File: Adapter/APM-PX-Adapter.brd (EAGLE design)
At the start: 22.9 x 20.3 mm, 13 parts, among them Q1 BSS138, Q2 BSS138

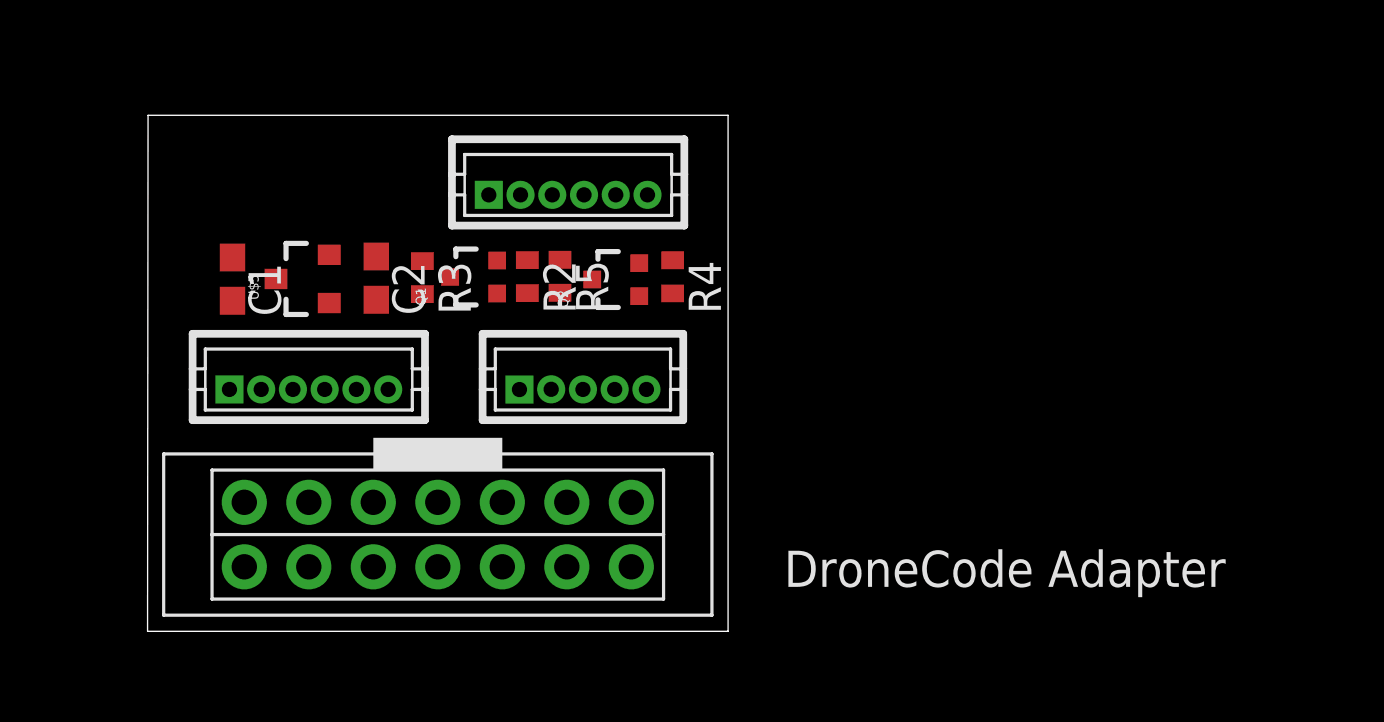
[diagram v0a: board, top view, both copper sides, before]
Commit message: Removed level shifting and switch to all through hole components. Ordering a prototype.
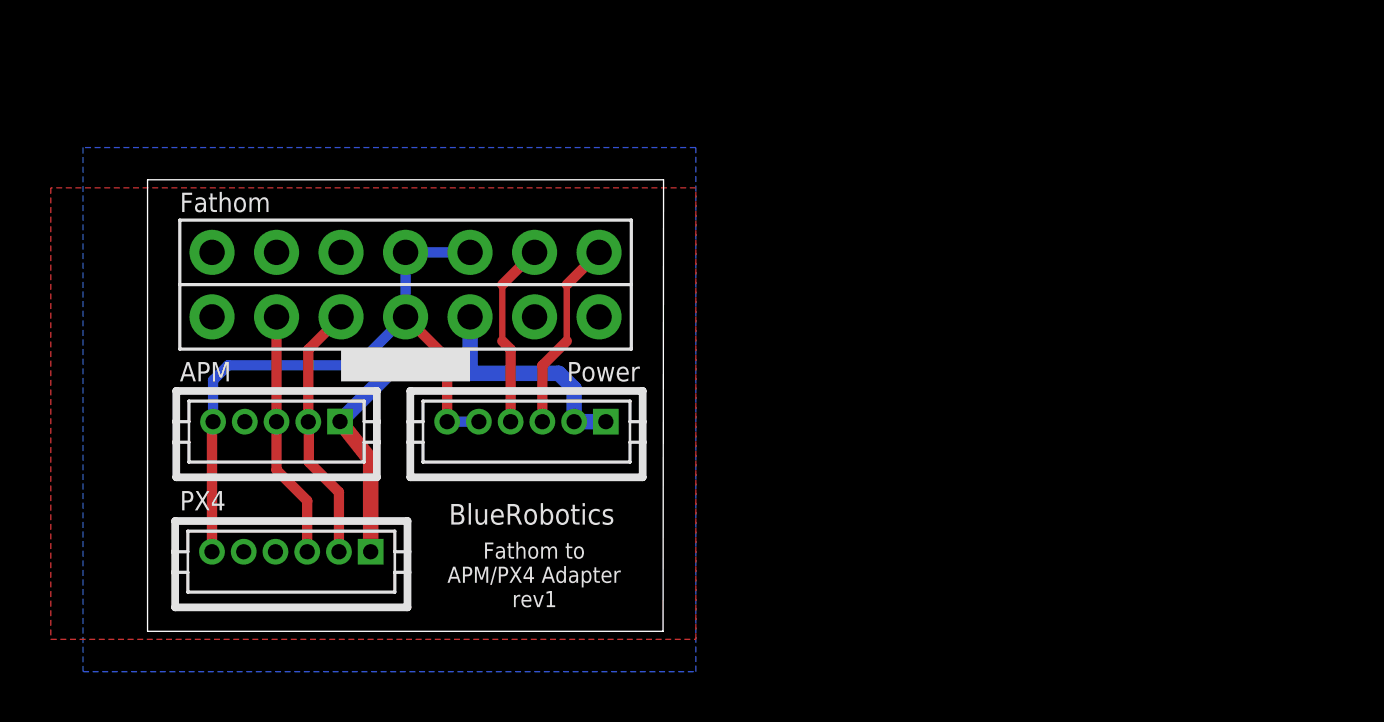
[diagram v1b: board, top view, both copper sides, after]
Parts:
- removed C1, C2: 1uF, resistor:C0603
- removed Q1, Q2: BSS138, SparkFun-DiscreteSemi:SOT323
- removed R2, R3, R4, R5: 10K, resistor:R0402
- removed U$5: AP7313-33SRG-7, BlueRobotics-Main:SOT23-3
- moved U$3 18.1 mm to (2.54, 12.4), turned to 0 degrees
- moved U$4 17.8 mm to (5.66, 3.13), turned to 0 degrees
- moved U$1 12.1 mm to (5.08, 8.26), turned to 0 degrees
- moved U$2 8.67 mm to (14.9, 8.26), turned to 0 degrees
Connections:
- removed net +3.3V: C2.1, Q1.1, Q2.1, R2.2, R4.2, U$5.2
- removed net RX3V3: Q2.2, R4.1, U$4.P$3
- removed net RX5V: Q2.3, R5.1, U$1.P$3, U$3.RX
- removed net TX3V3: Q1.2, R2.1, U$4.P$2
- removed net TX5V: Q1.3, R3.1, U$1.P$2, U$3.TX
- new net RX: U$1.P$3, U$3.RX, U$4.P$3
- new net TX: U$1.P$2, U$3.TX, U$4.P$2
- net +5V: no longer C1.1, R3.2, R5.2, U$5.3
- net GND: no longer C1.2, C2.2, U$5.1
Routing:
- net GND: track 0.00 -> 26.5 mm
- net +5V: track 0.00 -> 20.6 mm
- net TX: track 0.00 -> 10.3 mm
- net RX: track 0.00 -> 9.75 mm
- net I_SENSE: track 0.00 -> 7.59 mm
- net V_SENSE: track 0.00 -> 7.33 mm
- added copper zone on layer 1, net GND
- added copper zone on layer 16, net GND
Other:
- board size 22.9 x 20.3 mm -> 20.3 x 17.8 mm
- board text added: "APM"
- board text added: "Fathom"
- board text added: "Fathom to APM/PX4 Adapter"
- board text added: "PX4"
- board text added: "Power"
- board text added: "rev1"
- board text removed: "DroneCode Adapter"

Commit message: Updates to adapter board.
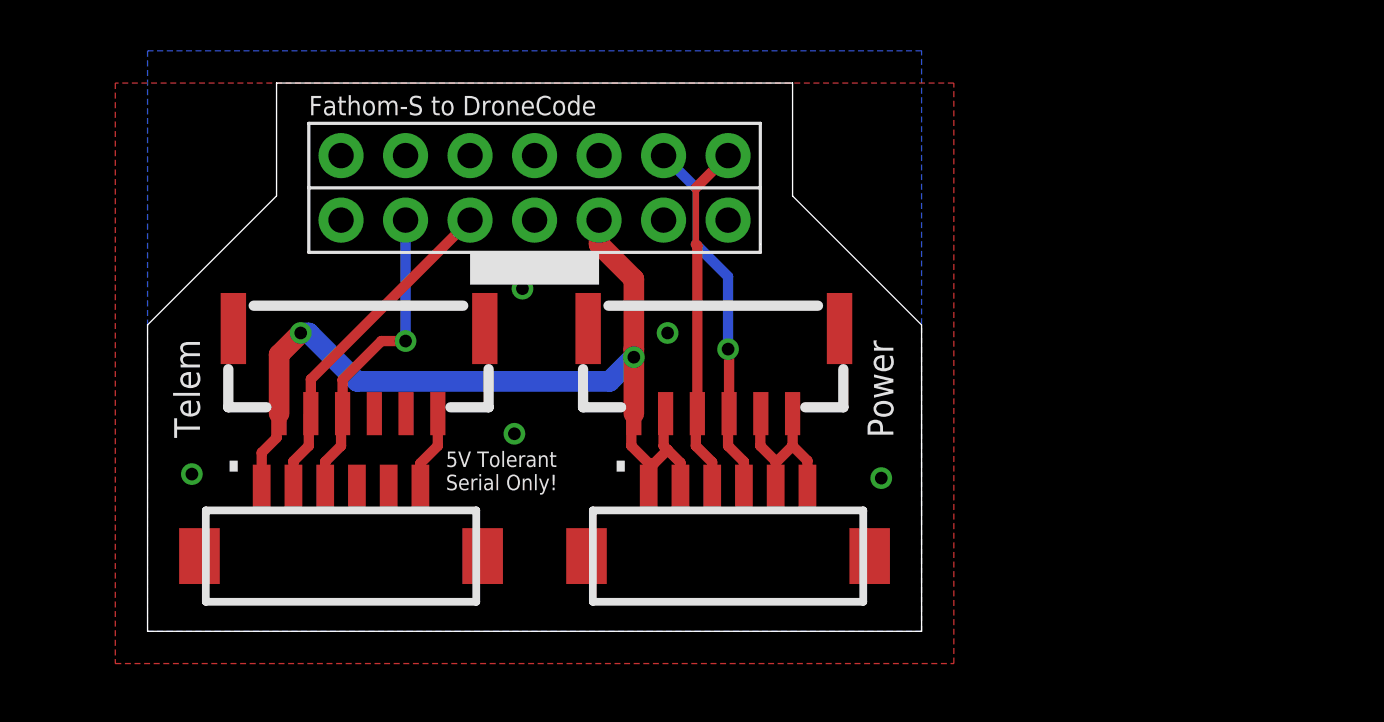
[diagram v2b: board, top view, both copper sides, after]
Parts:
- added U$5: JST-GH-6TOP-ENTRY, BlueRobotics-JST-GH:JST-GH-TOP-6
- U$1: value DF13-5P-1.25DSA -> JST-GH-6TOP-ENTRY; device con-hirose-df13:DF13-5P-1.25DSA -> BlueRobotics-JST-GH:JST-GH-TOP-6
- U$2, U$4: value DF13-6P-1.25DSA -> DF13-6P-1.25V; device con-hirose-df13:DF13-6P-1.25DSA -> con-hirose-df13:DF13C-6P-1.25V
- moved U$2 8.67 mm to (22.9, 4.76)
- moved U$1 6.36 mm to (11.4, 8.57), turned to 180 degrees
- moved U$3 6.35 mm to (7.62, 16.2)
- moved U$4 2.55 mm to (7.62, 4.76)
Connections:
- net +5V: now also U$1.1, U$5.1, U$5.2; no longer U$1.P$1
- net GND: now also U$1.6, U$5.5, U$5.6; no longer U$1.P$5
- net I_SENSE: now also U$5.3
- net RX: now also U$1.3; no longer U$1.P$3
- net TX: now also U$1.2; no longer U$1.P$2
- net V_SENSE: now also U$5.4
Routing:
- net GND: track 26.5 -> 10.4 mm, vias 0 -> 5
- net +5V: track 20.6 -> 36.6 mm, vias 0 -> 2
- net V_SENSE: track 7.33 -> 14.4 mm, vias 0 -> 1
- net I_SENSE: track 7.59 -> 13.9 mm
- net TX: track 10.3 -> 13.4 mm
- net RX: track 9.75 -> 12.4 mm, vias 0 -> 1
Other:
- board size 20.3 x 17.8 mm -> 30.5 x 21.6 mm
- board text added: "5V Tolerant Serial Only!"
- board text added: "Fathom-S to DroneCode"
- board text added: "Fathom-S to PixHawk Adapter"
- board text added: "Telem"
- board text added: "rev2"
- board text removed: "APM"
- board text removed: "Fathom"
- board text removed: "Fathom to APM/PX4 Adapter"
- board text removed: "PX4"
- board text removed: "rev1"
